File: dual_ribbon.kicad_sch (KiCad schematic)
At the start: 33 parts, among them Q1 PNP, Q2 MMBF4391, Q3 MMBF4391, U1 LM4041LP-ADJ, U2 TL074, U3 OPA2134, U4 TL074

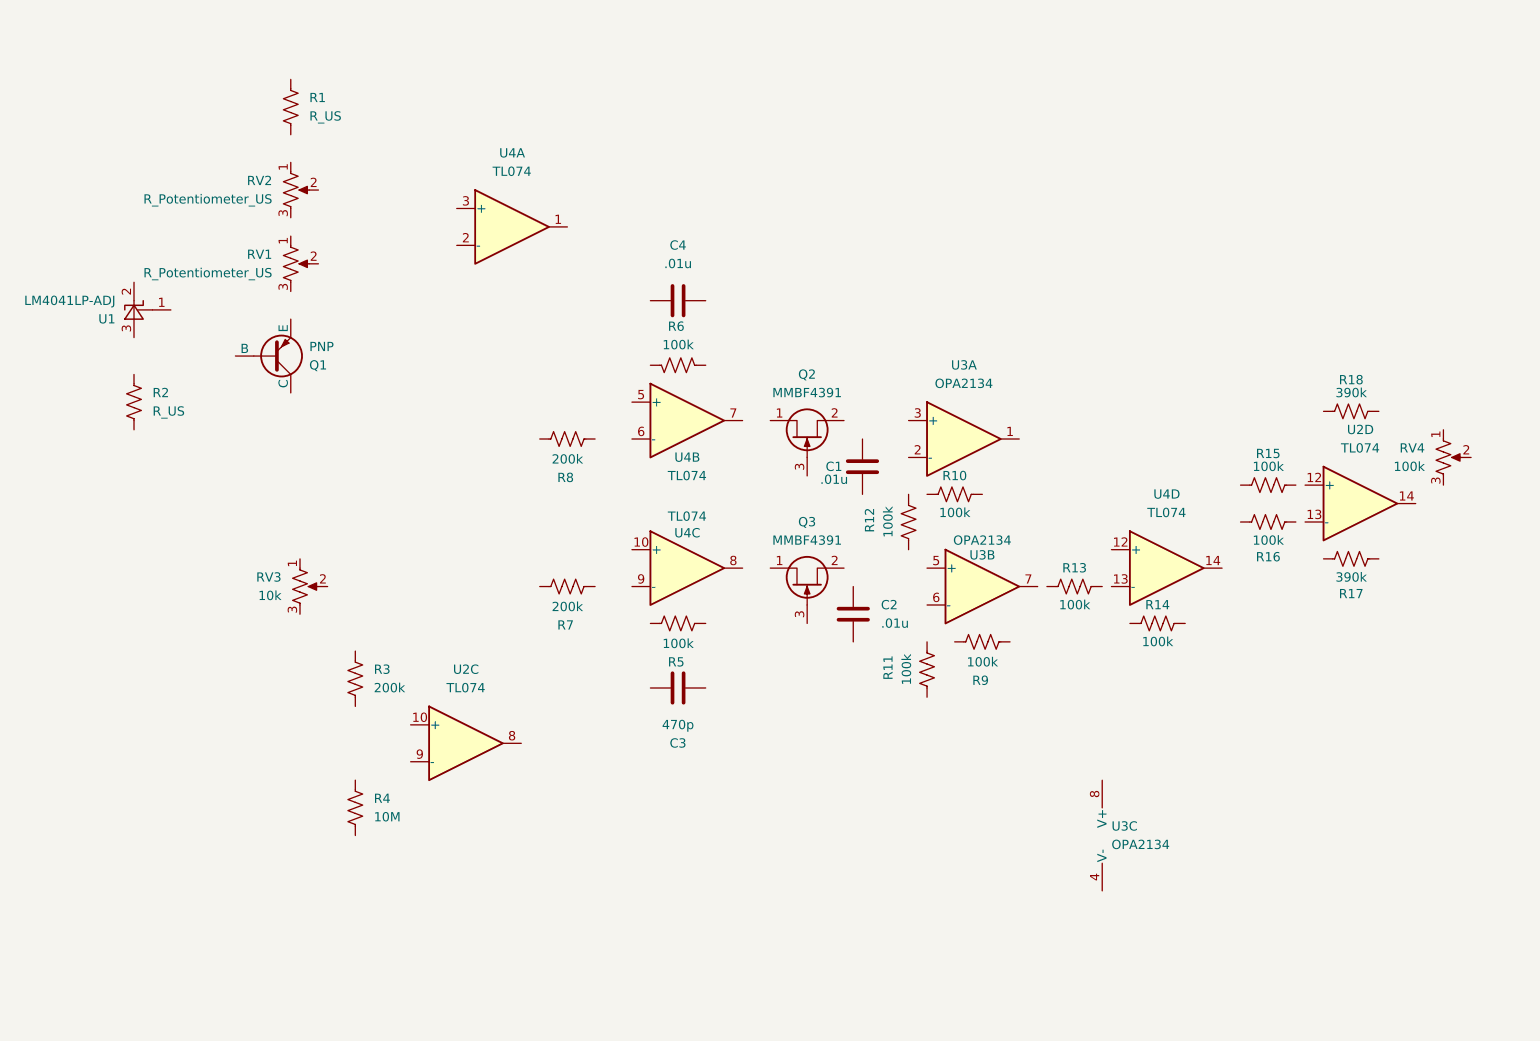
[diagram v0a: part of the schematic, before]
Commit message: Began wiring
Did not finish wiring
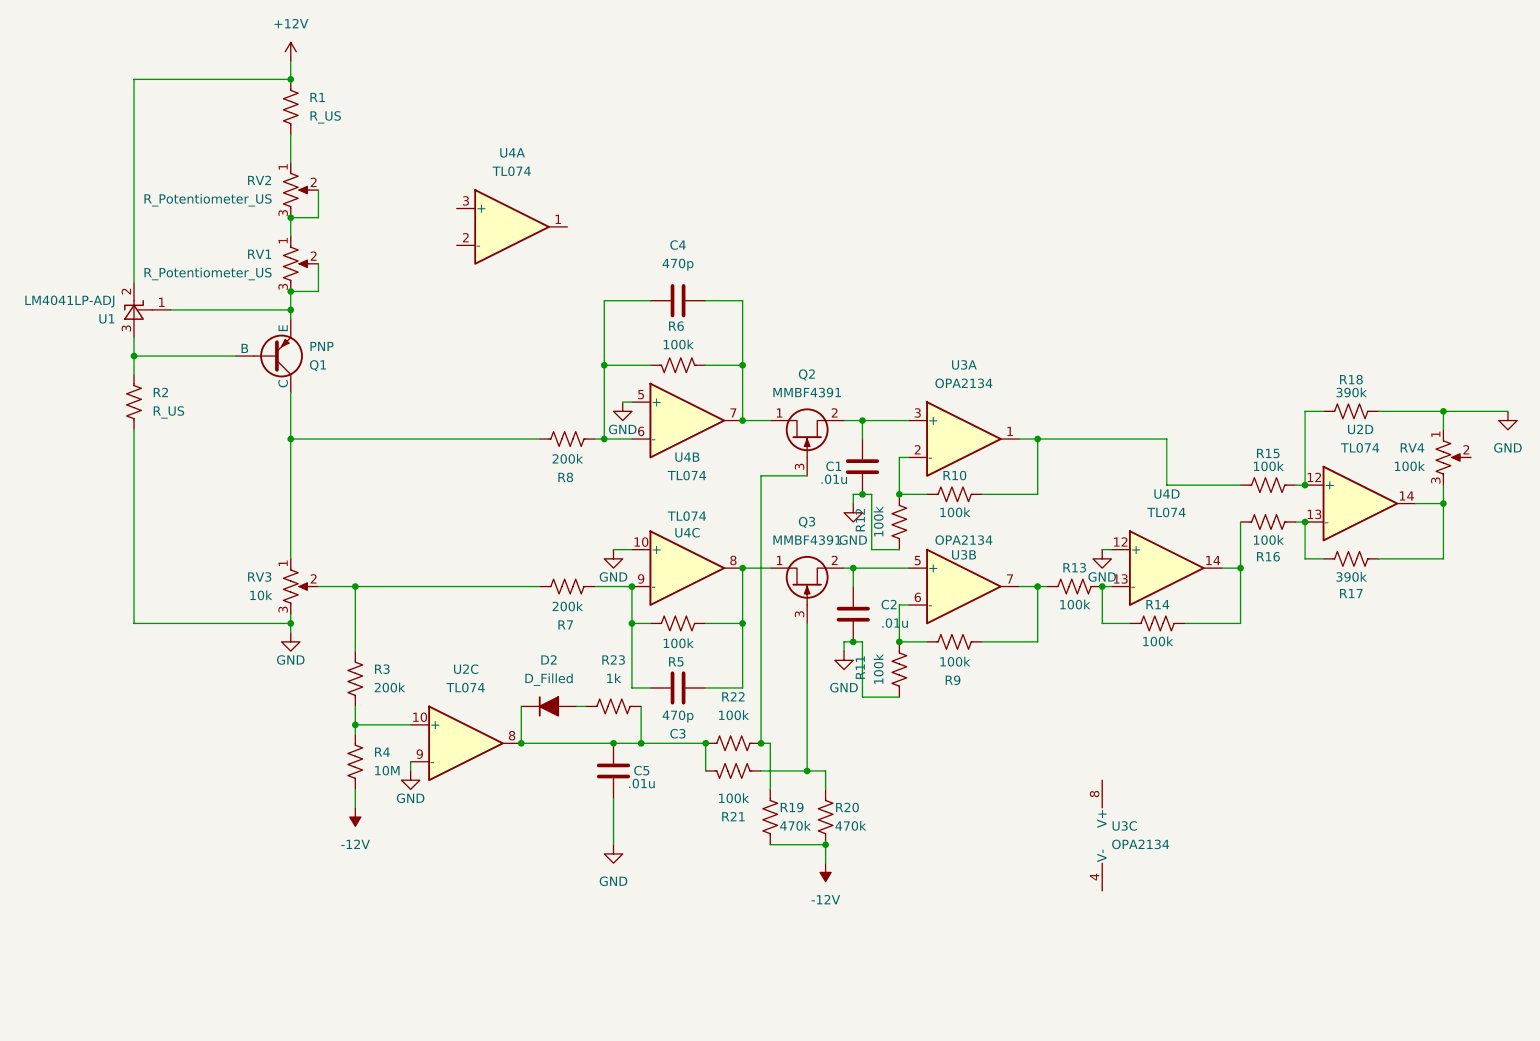
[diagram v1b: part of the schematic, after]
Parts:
- added C5: .01u, symbol Device:C
- added D2: D_Filled, symbol Device:D_Filled
- added R19, R20: 470k, symbol Device:R_US
- added R21, R22: 100k, symbol Device:R_US
- added R23: 1k, symbol Device:R_US
- C4: value .01u -> 470p
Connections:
- net at U2.12 (+): now also R15.2, R18.1
- net at U2.13 (-): now also R16.2, R17.1
- net at U2.14: now also R17.2, RV4.3
- net at Q2.1 (D): now also C4.2, R6.2, U4.7
- net at Q2.2 (S): now also C1.1, U3.3 (+)
- net at Q2.3 (G): now also R19.2, R22.2
- net at R4.1: now also R3.1, U2.10 (+)
- net -12V: now reaches R4.2
- net -12V: now also R19.1, R20.1
- net at R9.1: now also R11.1, U3.6 (-)
- net at R9.2: now also R13.1, U3.7
- net GND: now reaches R18.2
- net GND: now also C1.2, C2.2, R11.2, R12.2, R2.2, RV3.3, RV4.1, U2.9 (-), U4.10 (+), U4.12 (+), U4.5 (+), C5.2
- net at C3.1: now also Q3.1 (D), R5.2, U4.8
- net at C3.2: now also R5.1, R7.2, U4.9 (-)
- net at U4.6 (-): now also C4.1, R6.1, R8.2
- net at U3.5 (+): now also C2.1, Q3.2 (S)
- net at R10.1: now also R12.1, U3.2 (-)
- net at R10.2: now also R15.1, U3.1
- net at U1.1 (FB): now also Q1.3 (E), RV1.2, RV1.3
- net +12V: now reaches U1.2 (K)
- net +12V: now also R1.1
- net at U1.3 (A): now also Q1.2 (B), R2.1
- net at R3.2: now also R7.1, RV3.2
- net at Q1.1 (C): now also R8.1, RV3.1
- net at R1.2: now also RV2.1
- net at U2.8: now also C5.1, D2.1 (K), R21.1, R22.1, R23.2
- net at Q3.3 (G): now also R20.2, R21.2
- net at RV2.2: now also RV1.1, RV2.3
- net at R14.1: now also R13.2, U4.13 (-)
- net at R14.2: now also R16.1, U4.14
- new net: D2.2 (A), R23.1
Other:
- moved on the sheet: R11, R12, R4, R9, RV3, U3B

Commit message: Finish schematic and assign footprints
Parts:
- removed U2: TL074, symbol Amplifier_Operational:TL074
- added C10, C11, C6, C7, C8, C9: 100u, Capacitor_THT:CP_Radial_D6.3mm_P2.50mm, symbol Device:C_Polarized_US
- added D1: LED, LED_THT:LED_D3.0mm, symbol Device:LED
- added D3: 1N914, Diode_SMD:D_0805_2012Metric, symbol Device:D_Filled
- added J1, J2, J3, J4: Conn_01x02_Socket, Connector_Wire:SolderWire-0.75sqmm_1x02_P4.8mm_D1.25mm_OD2.3mm, symbol Connector:Conn_01x02_Socket
- added R24: 3.3k, Resistor_SMD:R_0805_2012Metric, symbol Device:R_US
- added U2: TL072, Package_SO:SOIC-10_3.9x4.9mm_P1mm, symbol Amplifier_Operational:TL072
- C1, C2, C5: footprint (none) -> Capacitor_THT:C_Rect_L7.2mm_W2.5mm_P5.00mm_FKS2_FKP2_MKS2_MKP2
- C3, C4: footprint (none) -> Capacitor_SMD:C_0805_2012Metric
- D2: value D_Filled -> 1N914; footprint (none) -> Diode_SMD:D_0805_2012Metric
- LEVEL1: renamed from RV4; footprint (none) -> Connector_Wire:SolderWire-0.75sqmm_1x03_P4.8mm_D1.25mm_OD2.3mm
- Q1: footprint (none) -> Package_TO_SOT_SMD:SOT-23
- R1: value R_US -> 500; footprint (none) -> Resistor_SMD:R_0805_2012Metric
- R10, R11, R12, R13, R14, R15, R16, R17, R18, R19, R20, R21, R22, R23, R3, R4, R5, R6, R7, R8, R9: footprint (none) -> Resistor_SMD:R_0805_2012Metric
- R2: value R_US -> 120k; footprint (none) -> Resistor_SMD:R_0805_2012Metric
- RANGE1: renamed from RV1; value R_Potentiometer_US -> 10k; footprint (none) -> Connector_Wire:SolderWire-0.75sqmm_1x03_P4.8mm_D1.25mm_OD2.3mm
- RIBBON1: renamed from RV3; footprint (none) -> Connector_Wire:SolderWire-0.75sqmm_1x03_P4.8mm_D1.25mm_OD2.3mm
- TRIM1: renamed from RV2; value R_Potentiometer_US -> 1k; footprint (none) -> Connector_Wire:SolderWire-0.75sqmm_1x03_P4.8mm_D1.25mm_OD2.3mm
- U3: footprint (none) -> Package_SO:SOIC-8_3.9x4.9mm_P1.27mm
- U4: footprint (none) -> Package_SO:SOIC-14_3.9x8.7mm_P1.27mm
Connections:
- net +12V: now also U3.8 (V+), U4.4 (V+), C10.1, C6.1, C8.1, U2.8 (V+)
- net -12V: now also U3.4 (V-), U4.11 (V-), C11.2, C7.2, C9.2, U2.4 (V-)
- net GND: now also U4.13 (-), U4.3 (+), U4.9 (-), C10.2, C11.1, C6.2, C7.1, C8.2, C9.1, D1.1 (K), J1.1 (Pin_1), J2.1 (Pin_1), J3.1 (Pin_1), J4.1 (Pin_1), U2.3 (+); no longer U4.10 (+), U4.12 (+)
- net at R15.2, R18.1: now also U2.5 (+)
- net at R16.2, R17.1: now also U2.6 (-)
- net at LEVEL1.3, R17.2: now also U2.7
- net at R3.1, R4.1: now also U4.10 (+)
- net at C3.1, Q3.1 (D), R5.2: now also U4.1; no longer U4.8
- net at C3.2, R5.1, R7.2: now also U4.2 (-); no longer U4.9 (-)
- net at R10.2, R15.1, U3.1: now also J1.2 (Pin_2)
- net at C5.1, D2.1 (K), R21.1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: now also U4.12 (+), U4.8
- net at LEVEL1.2: now also J2.2 (Pin_2)
- net at R13.2, R14.1: now also U2.2 (-); no longer U4.13 (-)
- net at R14.2, R16.1: now also J3.2 (Pin_2), U2.1; no longer U4.14
- new net: D1.2 (A), R24.2
- new net: D3.1 (K), J4.2 (Pin_2)
- new net: D3.2 (A), R24.1, U4.14
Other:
- moved on the sheet: U3C, U4A, U4C, U4D, U4E

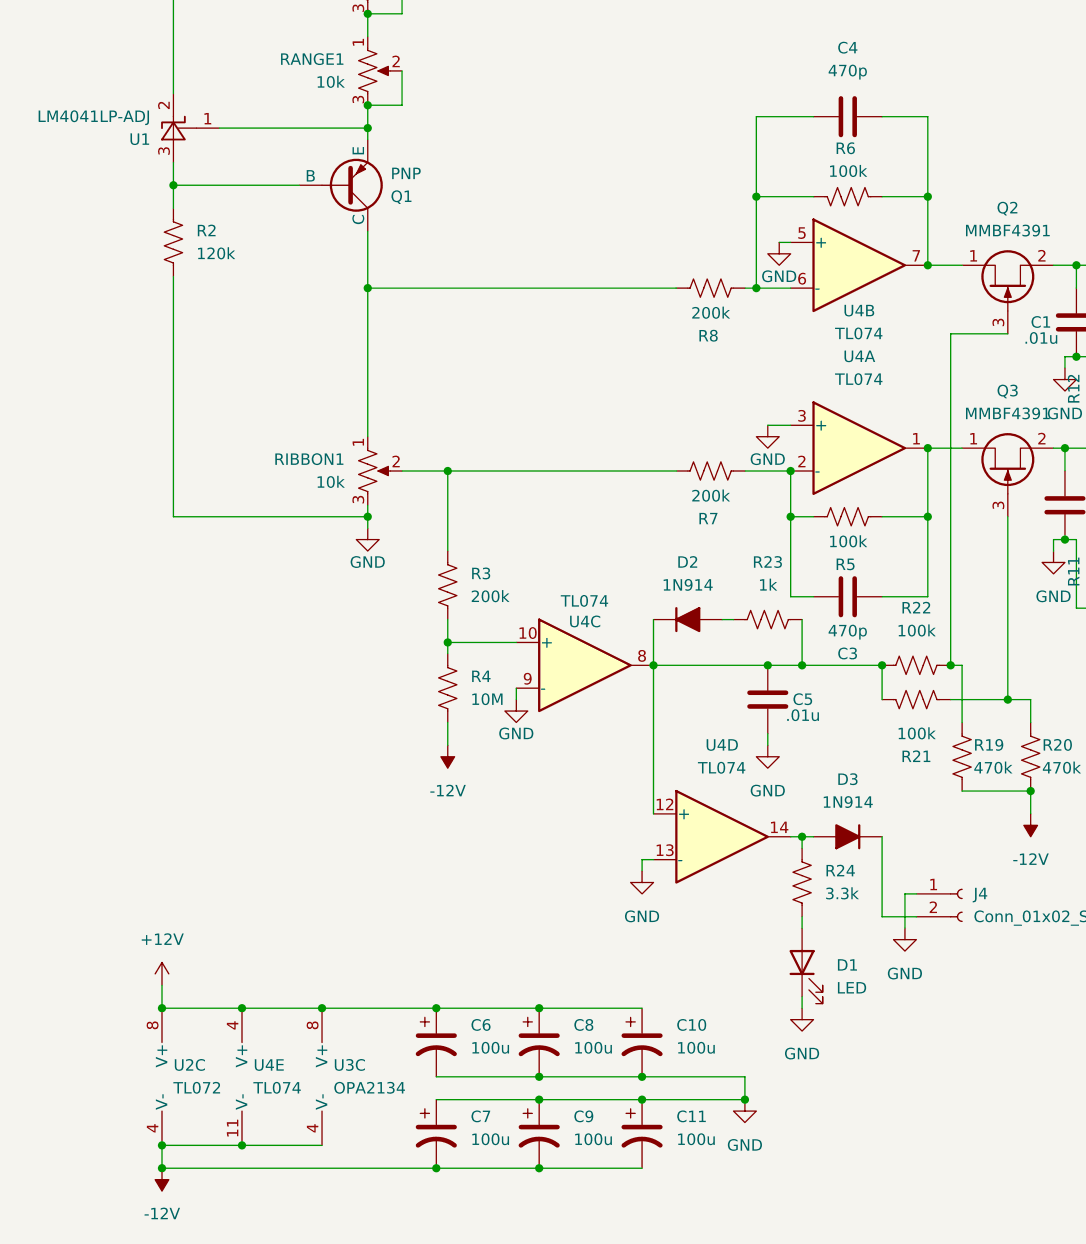
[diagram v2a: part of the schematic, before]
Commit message: Minor schematic fixes
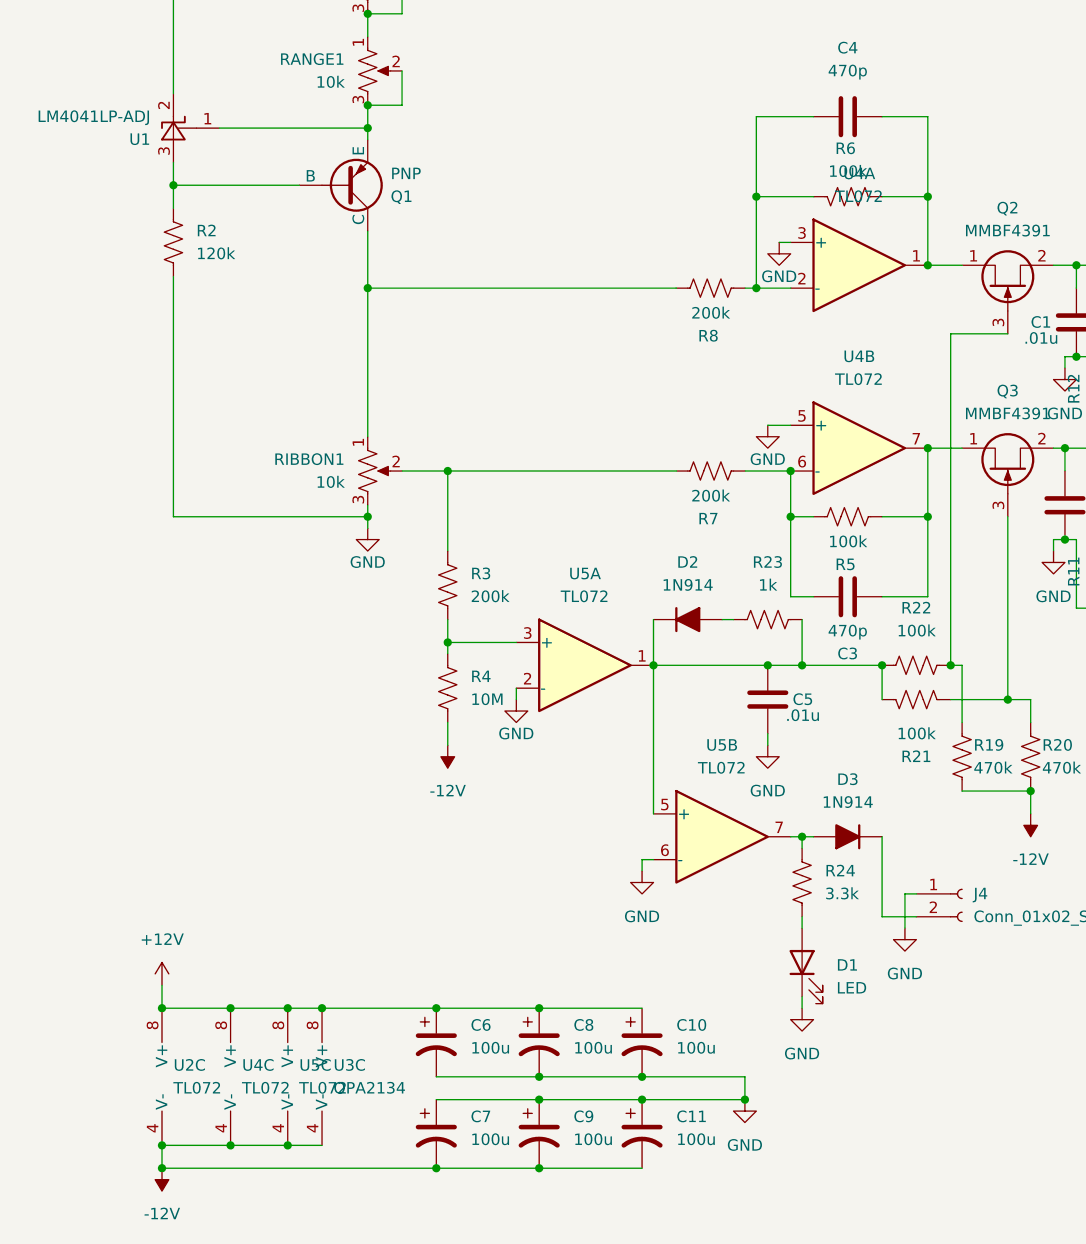
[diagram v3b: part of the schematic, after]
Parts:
- removed U4: TL074, Package_SO:SOIC-14_3.9x8.7mm_P1.27mm, symbol Amplifier_Operational:TL074
- added U4, U5: TL072, Package_SO:SOIC-8_3.9x4.9mm_P1.27mm, symbol Amplifier_Operational:TL072
- U2: footprint Package_SO:SOIC-10_3.9x4.9mm_P1mm -> Package_SO:SOIC-8_3.9x4.9mm_P1.27mm
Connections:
- net +12V: now also U4.8 (V+), U5.8 (V+)
- net -12V: now also U4.4 (V-), U5.4 (V-)
- net GND: now also U4.3 (+), U4.5 (+), U5.2 (-), U5.6 (-)
- net at C4.2, Q2.1 (D), R6.2: now also U4.1
- net at R3.1, R4.1: now also U5.3 (+)
- net at C3.1, Q3.1 (D), R5.2: now also U4.7
- net at C3.2, R5.1, R7.2: now also U4.6 (-)
- net at C4.1, R6.1, R8.2: now also U4.2 (-)
- net at C5.1, D2.1 (K), R21.1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: now also U5.1, U5.5 (+)
- net at D3.2 (A), R24.1: now also U5.7
